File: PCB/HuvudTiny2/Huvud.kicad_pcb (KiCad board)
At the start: 4 copper layers, 42 x 42 mm, 99 parts, among them J1 Vin, J12 USB_Micro-B, J2 DBG, J3 THERM, J4 FAN0, J5 FAN1, J6 Heater, J7 Endstop, J9 STEPPER, Q1 AO3400A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

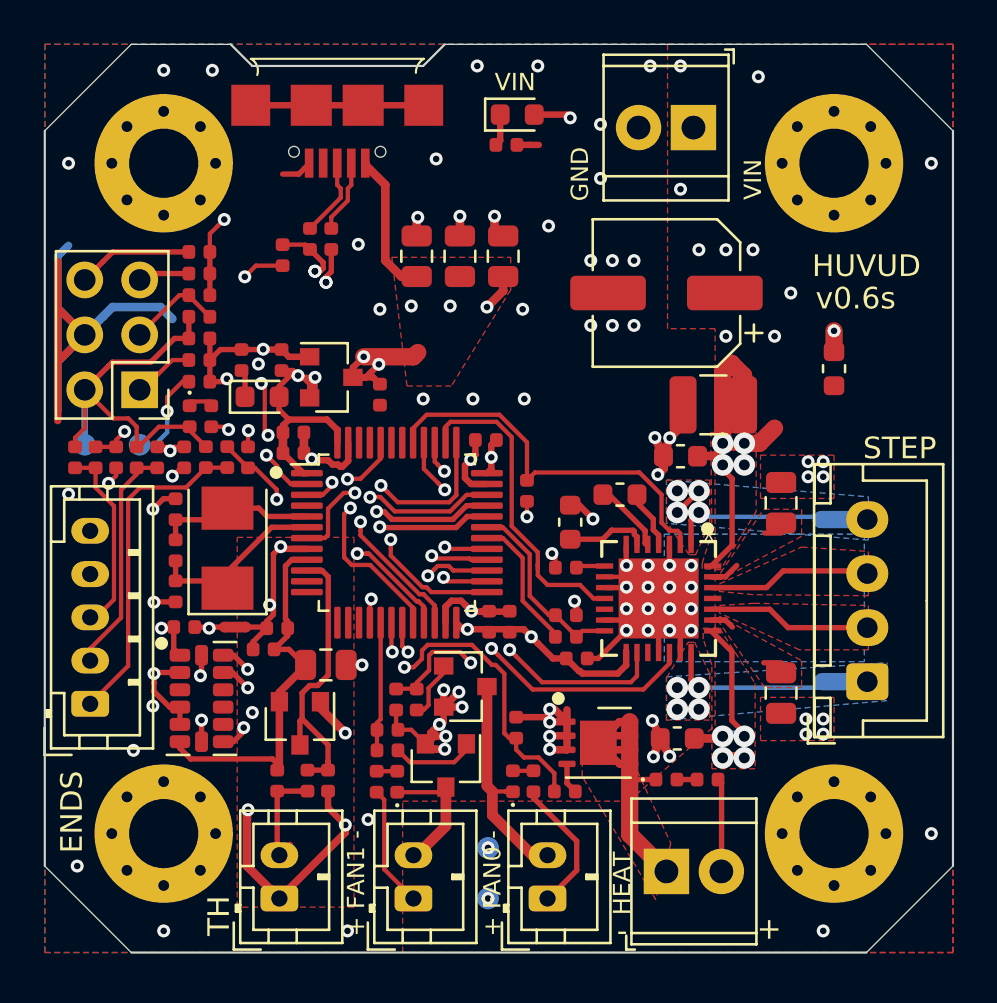
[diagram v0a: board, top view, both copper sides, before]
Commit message: Add protection diode on endstop 1. Add back heatsink for power mosfet.
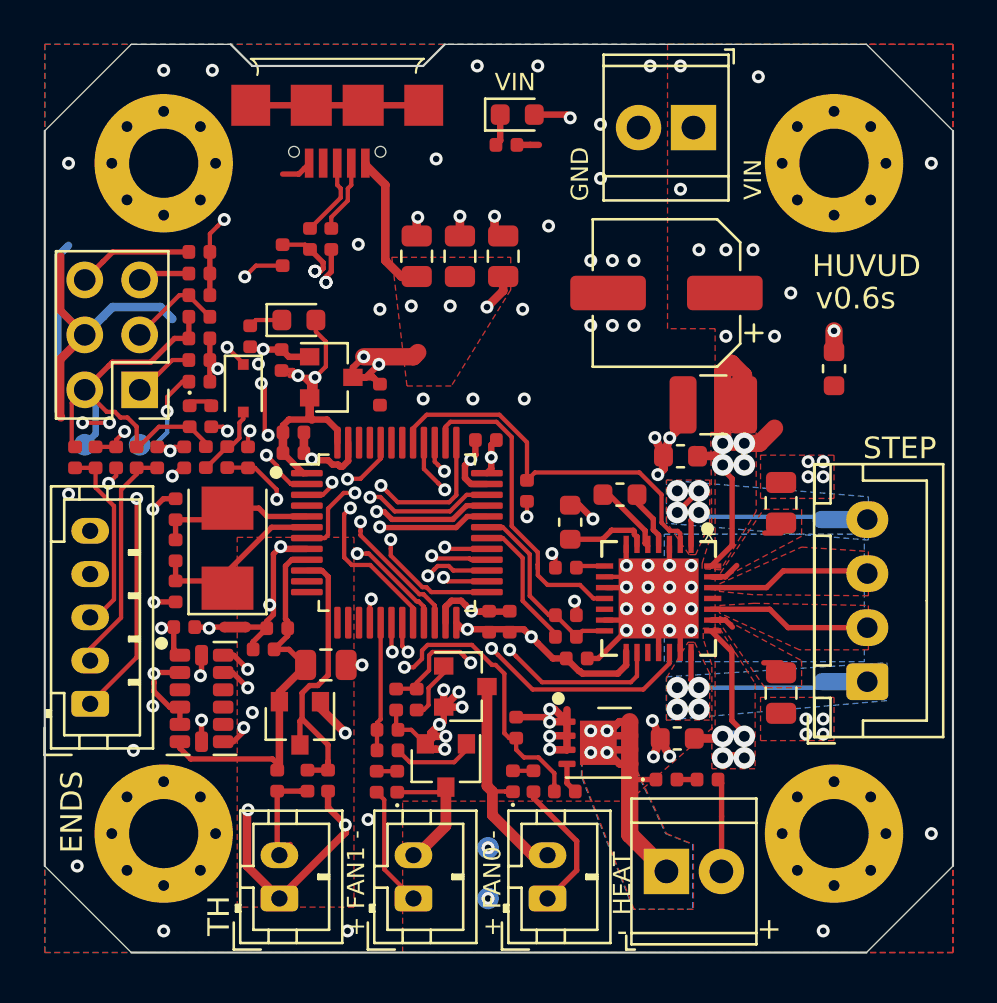
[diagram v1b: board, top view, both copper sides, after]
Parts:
- added D4: PMEG6010CEJ, Diode_SMD:D_SOD-323F, F.Cu at (191.2, 115.9)
- moved D8 3.94 mm to (193.8, 112.8)
- moved R20 1.17 mm to (191.5, 113.5), turned to -90 degrees
- turned R32 to -90 degrees
- turned R33 to -90 degrees
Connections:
- J7 pad 1: Net-(J7-Pad1) -> Net-(D4-Pad1)
- R32 pad 1: Net-(J7-Pad1) -> +3V3
- R32 pad 2: +3V3 -> Net-(D4-Pad2)
- R33 pad 1: Net-(J7-Pad1) -> Net-(D4-Pad2)
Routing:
- net Net-(D4-Pad1): track 0.00 -> 32.0 mm, vias 0 -> 4
- net Net-(J7-Pad1): track 15.4 -> 0.00 mm
- net GND: track 122.3 -> 116.9 mm
- net Net-(D4-Pad2): track 0.00 -> 3.40 mm
- net +3V3: track 85.3 -> 87.7 mm
- net SWCLK: track 32.3 -> 33.0 mm
- net Net-(D3-Pad1): vias 0 -> 4
- added copper zone on B.Cu, net Net-(D3-Pad1)

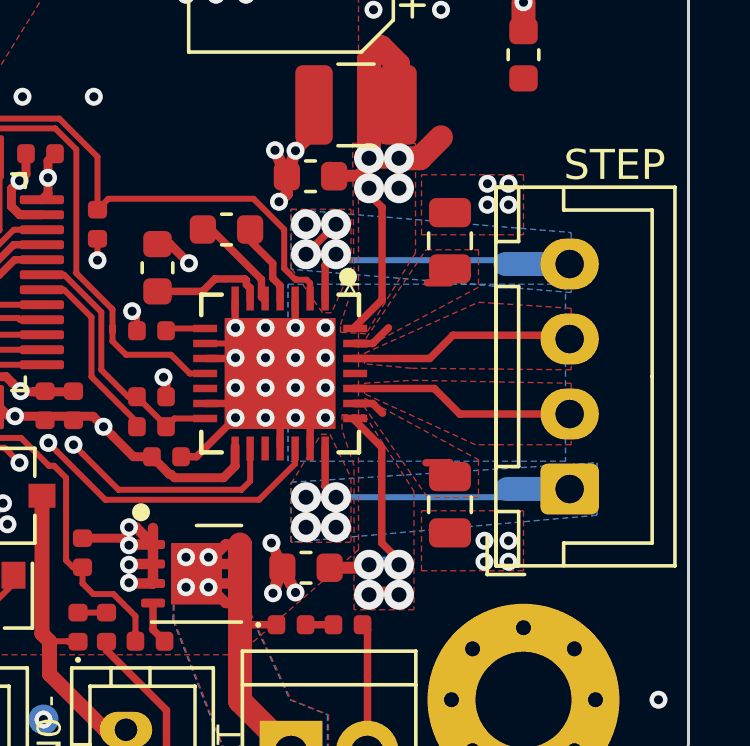
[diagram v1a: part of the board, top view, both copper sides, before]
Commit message: Update sense resistors to 0.1 1206 size.
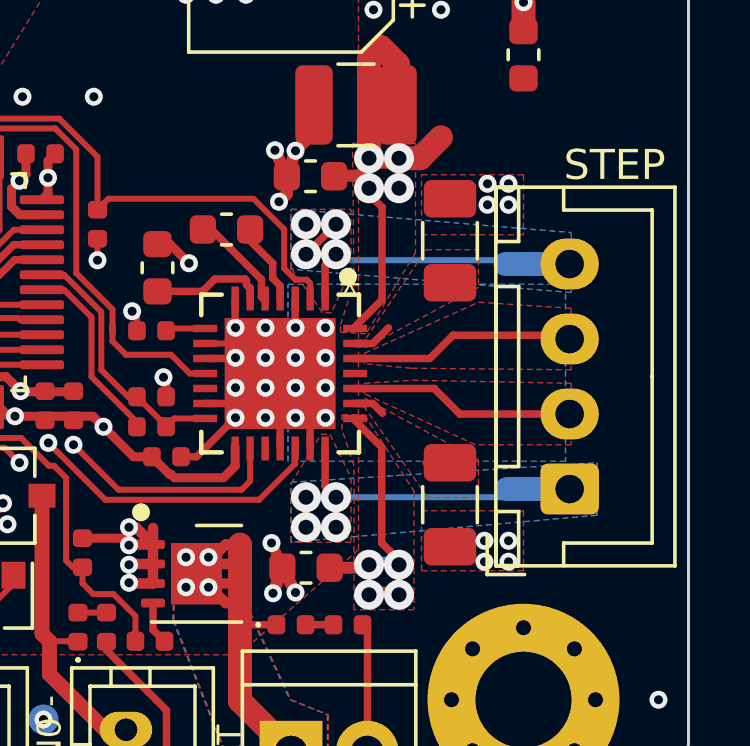
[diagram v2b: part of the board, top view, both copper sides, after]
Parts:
- R4, R7: value 0.110 1% -> 0.1 1%; footprint Resistor_SMD:R_0805_2012Metric -> Resistor_SMD:R_1206_3216Metric
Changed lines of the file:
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@@
     )
   )
-  (footprint "Resistor_SMD:R_0805_2012Metric" (layer "F.Cu")
+  (footprint "Resistor_SMD:R_1206_3216Metric" (layer "F.Cu")
     (at 216.05 121.2 -90)
-    (descr "Resistor SMD 0805 (2012 Metric), square (rectangular) end terminal, IPC_7351 nominal, (Body size source: https://docs.google.com/spreadsheets/d/1BsfQQcO9C6DZCsRaXUlFlo91Tg2WpOkGARC1WS5S8t0/edit?usp=sharing), generated with kicad-footprint-generator")
+    (descr "Resistor SMD 1206 (3216 Metric), square (rectangular) end terminal, IPC_7351 nominal, (Body size source: http://www.tortai-tech.com/upload/download/2011102023233369053.pdf), generated with kicad-footprint-generator")
     (tags "resistor")
-    (property "LCSC" "C53899")
-    (property "Sheetfile" "Huvud.kicad_sch")
-    (property "Sheetname" "")
-    (attr smd)
-    (fp_text reference "R7" (at 0 -1.65 -90) (layer "F.SilkS") hide
-      (effects (font (size 1 1) (thickness 0.15)))
-    )
-    (fp_text value "0.110 1%" (at 0 1.65 -90) (layer "F.Fab")
+    (property "LCSC" "C25334")
+    (property "Sheetfile" "Huvud.kicad_sch")
+    (property "Sheetname" "")
+    (attr smd)
+    (fp_text reference "R7" (at 0 -1.82 -90) (layer "F.SilkS") hide
+      (effects (font (size 1 1) (thickness 0.15)))
+    )
+    (fp_text value "0.1 1%" (at 0 1.82 -90) (layer "F.Fab")
       (effects (font (size 1 1) (thickness 0.15)))
     )
     (fp_text user "${REFERENCE}" (at 0 0 -90) (layer "F.Fab")
-      (effects (font (size 0.5 0.5) (thickness 0.08)))
-    )
-    (fp_line (start -0.258578 -0.71) (end 0.258578 -0.71) (layer "F.SilkS") (width 0.12))
-    (fp_line (start -0.258578 0.71) (end 0.258578 0.71) (layer "F.SilkS") (width 0.12))
-    (fp_line (start 1.68 0.95) (end -1.68 0.95) (layer "F.CrtYd") (width 0.05))
-    (fp_line (start 1.68 -0.95) (end 1.68 0.95) (layer "F.CrtYd") (width 0.05))
-    (fp_line (start -1.68 -0.95) (end 1.68 -0.95) (layer "F.CrtYd") (width 0.05))
-    (fp_line (start -1.68 0.95) (end -1.68 -0.95) (layer "F.CrtYd") (width 0.05))
-    (fp_line (start 1 0.6) (end -1 0.6) (layer "F.Fab") (width 0.1))
-    (fp_line (start -1 -0.6) (end 1 -0.6) (layer "F.Fab") (width 0.1))
-    (fp_line (start -1 0.6) (end -1 -0.6) (layer "F.Fab") (width 0.1))
-    (fp_line (start 1 -0.6) (end 1 0.6) (layer "F.Fab") (width 0.1))
-    (pad "1" smd roundrect locked (at -0.9375 0 270) (size 0.975 1.4) (layers "F.Cu" "F.Paste" "F.Mask") (roundrect_rratio 0.25)
+      (effects (font (size 0.8 0.8) (thickness 0.12)))
+    )
+    (fp_line (start -0.602064 -0.91) (end 0.602064 -0.91) (layer "F.SilkS") (width 0.12))
+    (fp_line (start -0.602064 0.91) (end 0.602064 0.91) (layer "F.SilkS") (width 0.12))
+    (fp_line (start 2.28 -1.12) (end 2.28 1.12) (layer "F.CrtYd") (width 0.05))
+    (fp_line (start 2.28 1.12) (end -2.28 1.12) (layer "F.CrtYd") (width 0.05))
+    (fp_line (start -2.28 -1.12) (end 2.28 -1.12) (layer "F.CrtYd") (width 0.05))
+    (fp_line (start -2.28 1.12) (end -2.28 -1.12) (layer "F.CrtYd") (width 0.05))
+    (fp_line (start -1.6 0.8) (end -1.6 -0.8) (layer "F.Fab") (width 0.1))
+    (fp_line (start 1.6 -0.8) (end 1.6 0.8) (layer "F.Fab") (width 0.1))
+    (fp_line (start -1.6 -0.8) (end 1.6 -0.8) (layer "F.Fab") (width 0.1))
+    (fp_line (start 1.6 0.8) (end -1.6 0.8) (layer "F.Fab") (width 0.1))
+    (pad "1" smd roundrect locked (at -1.4 0 270) (size 1.25 1.75) (layers "F.Cu" "F.Paste" "F.Mask") (roundrect_rratio 0.2)
       (net 2 "GND") (pintype "passive"))
-    (pad "2" smd roundrect locked (at 0.9375 0 270) (size 0.975 1.4) (layers "F.Cu" "F.Paste" "F.Mask") (roundrect_rratio 0.25)
+    (pad "2" smd roundrect locked (at 1.4 0 270) (size 1.25 1.75) (layers "F.Cu" "F.Paste" "F.Mask") (roundrect_rratio 0.2)
       (net 32 "BRB") (pintype "passive"))
-    (model "${KISYS3DMOD}/Resistor_SMD.3dshapes/R_0805_2012Metric.wrl"
-      (offset (xyz 0 0 0))
-      (scale (xyz 1 1 1))
-      (rotate (xyz 0 0 0))
-    )
-  )
-  (footprint "Resistor_SMD:R_0805_2012Metric" (layer "F.Cu")
+    (model "${KISYS3DMOD}/Resistor_SMD.3dshapes/R_1206_3216Metric.wrl"
+      (offset (xyz 0 0 0))
+      (scale (xyz 1 1 1))
+      (rotate (xyz 0 0 0))
+    )
+  )
+  (footprint "Resistor_SMD:R_1206_3216Metric" (layer "F.Cu")
     (at 216.05 130 90)
-    (descr "Resistor SMD 0805 (2012 Metric), square (rectangular) end terminal, IPC_7351 nominal, (Body size source: https://docs.google.com/spreadsheets/d/1BsfQQcO9C6DZCsRaXUlFlo91Tg2WpOkGARC1WS5S8t0/edit?usp=sharing), generated with kicad-footprint-generator")
+    (descr "Resistor SMD 1206 (3216 Metric), square (rectangular) end terminal, IPC_7351 nominal, (Body size source: http://www.tortai-tech.com/upload/download/2011102023233369053.pdf), generated with kicad-footprint-generator")
     (tags "resistor")
-    (property "LCSC" "C53899")
-    (property "Sheetfile" "Huvud.kicad_sch")
-    (property "Sheetname" "")
-    (attr smd)
-    (fp_text reference "R4" (at 0 -1.65 90) (layer "F.SilkS") hide
-      (effects (font (size 1 1) (thickness 0.15)))
-    )
-    (fp_text value "0.110 1%" (at 0 1.65 90) (layer "F.Fab")
+    (property "LCSC" "C25334")
+    (property "Sheetfile" "Huvud.kicad_sch")
+    (property "Sheetname" "")
+    (attr smd)
+    (fp_text reference "R4" (at 0 -1.82 90) (layer "F.SilkS") hide
+      (effects (font (size 1 1) (thickness 0.15)))
+    )
+    (fp_text value "0.1 1%" (at 0 1.82 90) (layer "F.Fab")
       (effects (font (size 1 1) (thickness 0.15)))
     )
     (fp_text user "${REFERENCE}" (at 0 0 90) (layer "F.Fab")
-      (effects (font (size 0.5 0.5) (thickness 0.08)))
-    )
-    (fp_line (start -0.258578 -0.71) (end 0.258578 -0.71) (layer "F.SilkS") (width 0.12))
-    (fp_line (start -0.258578 0.71) (end 0.258578 0.71) (layer "F.SilkS") (width 0.12))
-    (fp_line (start -1.68 -0.95) (end 1.68 -0.95) (layer "F.CrtYd") (width 0.05))
-    (fp_line (start -1.68 0.95) (end -1.68 -0.95) (layer "F.CrtYd") (width 0.05))
-    (fp_line (start 1.68 0.95) (end -1.68 0.95) (layer "F.CrtYd") (width 0.05))
-    (fp_line (start 1.68 -0.95) (end 1.68 0.95) (layer "F.CrtYd") (width 0.05))
-    (fp_line (start -1 -0.6) (end 1 -0.6) (layer "F.Fab") (width 0.1))
-    (fp_line (start 1 0.6) (end -1 0.6) (layer "F.Fab") (width 0.1))
-    (fp_line (start -1 0.6) (end -1 -0.6) (layer "F.Fab") (width 0.1))
-    (fp_line (start 1 -0.6) (end 1 0.6) (layer "F.Fab") (width 0.1))
-    (pad "1" smd roundrect locked (at -0.9375 0 90) (size 0.975 1.4) (layers "F.Cu" "F.Paste" "F.Mask") (roundrect_rratio 0.25)
+      (effects (font (size 0.8 0.8) (thickness 0.12)))
+    )
+    (fp_line (start -0.602064 -0.91) (end 0.602064 -0.91) (layer "F.SilkS") (width 0.12))
+    (fp_line (start -0.602064 0.91) (end 0.602064 0.91) (layer "F.SilkS") (width 0.12))
+    (fp_line (start -2.28 -1.12) (end 2.28 -1.12) (layer "F.CrtYd") (width 0.05))
+    (fp_line (start 2.28 1.12) (end -2.28 1.12) (layer "F.CrtYd") (width 0.05))
+    (fp_line (start 2.28 -1.12) (end 2.28 1.12) (layer "F.CrtYd") (width 0.05))
+    (fp_line (start -2.28 1.12) (end -2.28 -1.12) (layer "F.CrtYd") (width 0.05))
+    (fp_line (start -1.6 0.8) (end -1.6 -0.8) (layer "F.Fab") (width 0.1))
+    (fp_line (start 1.6 0.8) (end -1.6 0.8) (layer "F.Fab") (width 0.1))
+    (fp_line (start -1.6 -0.8) (end 1.6 -0.8) (layer "F.Fab") (width 0.1))
+    (fp_line (start 1.6 -0.8) (end 1.6 0.8) (layer "F.Fab") (width 0.1))
+    (pad "1" smd roundrect locked (at -1.4 0 90) (size 1.25 1.75) (layers "F.Cu" "F.Paste" "F.Mask") (roundrect_rratio 0.2)
       (net 2 "GND") (pintype "passive"))
-    (pad "2" smd roundrect locked (at 0.9375 0 90) (size 0.975 1.4) (layers "F.Cu" "F.Paste" "F.Mask") (roundrect_rratio 0.25)
+    (pad "2" smd roundrect locked (at 1.4 0 90) (size 1.25 1.75) (layers "F.Cu" "F.Paste" "F.Mask") (roundrect_rratio 0.2)
       (net 31 "BRA") (pintype "passive"))
-    (model "${KISYS3DMOD}/Resistor_SMD.3dshapes/R_0805_2012Metric.wrl"
+    (model "${KISYS3DMOD}/Resistor_SMD.3dshapes/R_1206_3216Metric.wrl"
       (offset (xyz 0 0 0))
       (scale (xyz 1 1 1))
@@
     (fp_line (start -0.5 0.25) (end -0.5 -0.25) (layer "F.Fab") (width 0.1))
     (pad "1" smd roundrect locked (at -0.485 0 270) (size 0.59 0.64) (layers "F.Cu" "F.Paste" "F.Mask") (roundrect_rratio 0.25)
-      (net 8 "+3V3"))
+      (net 8 "+3V3") (pintype "passive"))
     (pad "2" smd roundrect locked (at 0.485 0 270) (size 0.59 0.64) (layers "F.Cu" "F.Paste" "F.Mask") (roundrect_rratio 0.25)
-      (net 65 "Net-(D4-Pad2)"))
+      (net 65 "Net-(D4-Pad2)") (pintype "passive"))
     (model "${KISYS3DMOD}/Resistor_SMD.3dshapes/R_0402_1005Metric.wrl"
       (offset (xyz 0 0 0))

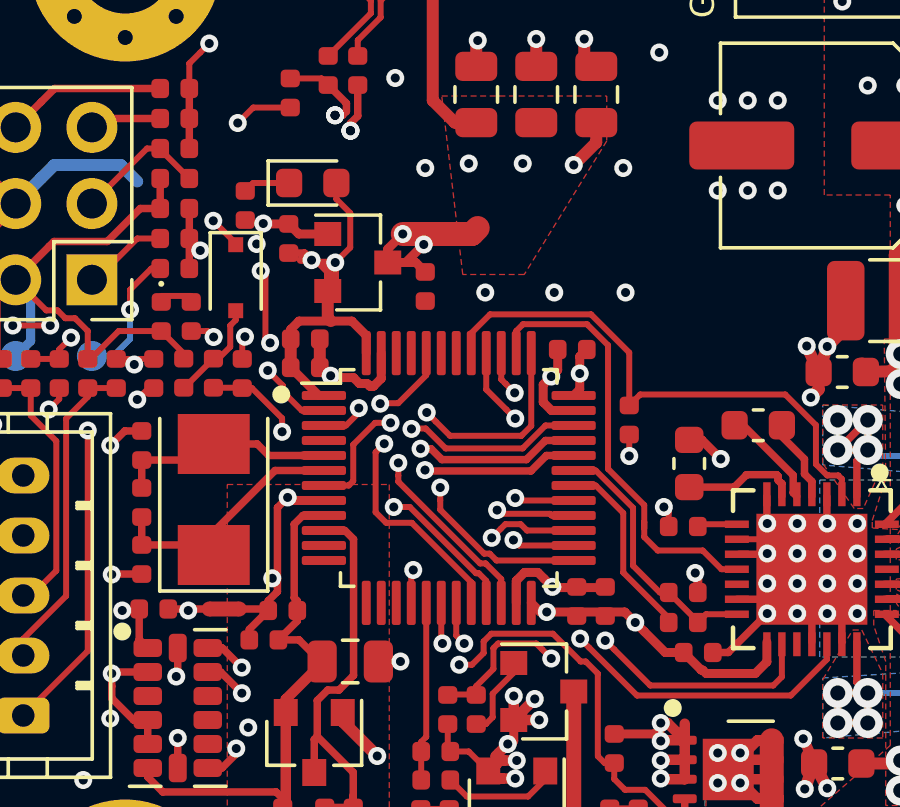
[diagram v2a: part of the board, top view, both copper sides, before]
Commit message: Route VCC_IO to GPIO pin so we can reset the stepper driver.
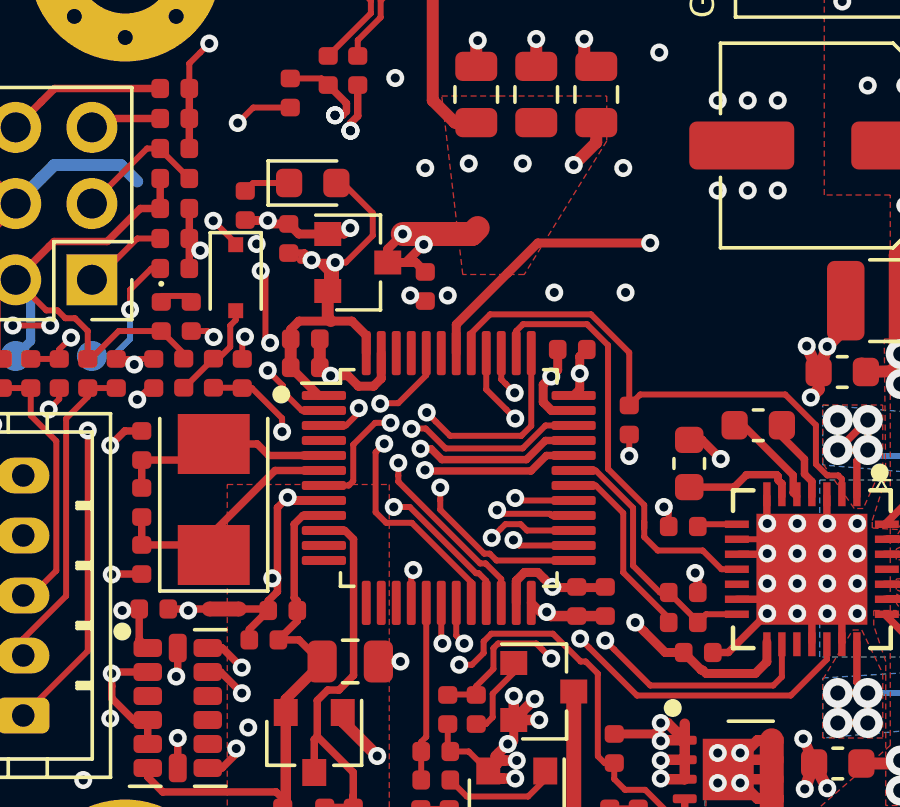
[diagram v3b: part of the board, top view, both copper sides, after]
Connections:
- C9 pad 2: +3V3 -> VCC_IO
- U2 pad 15: +3V3 -> VCC_IO
- U5 pad 42: (no net) -> VCC_IO
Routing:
- net VCC_IO: track 0.00 -> 27.3 mm, vias 0 -> 2
- net +3V3: track 87.7 -> 81.7 mm, vias 8 -> 7
- net GND: track 116.9 -> 118.4 mm, vias 90 -> 92

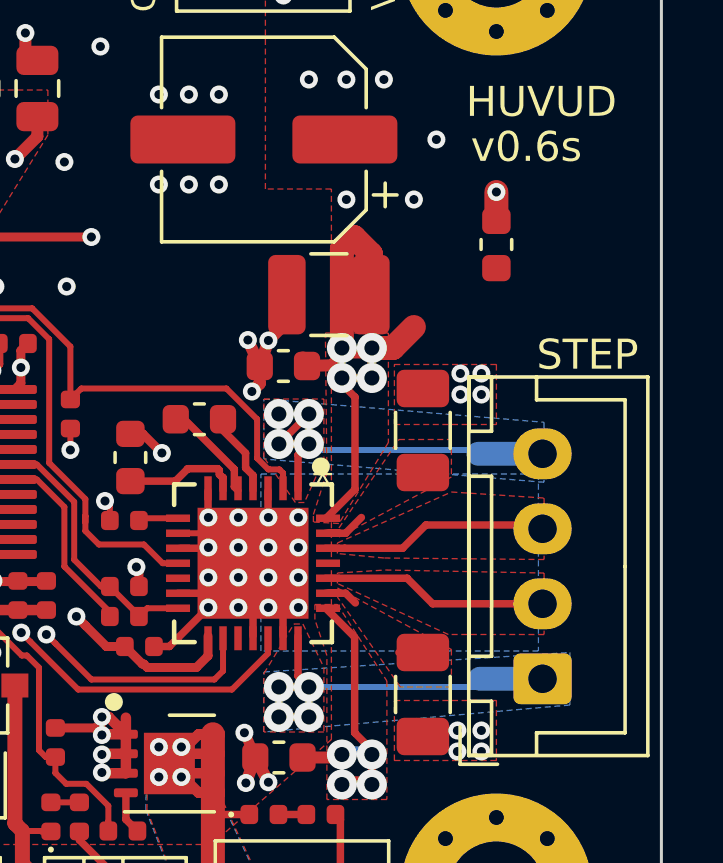
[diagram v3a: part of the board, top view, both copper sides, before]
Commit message: Added caps across stepper pins.
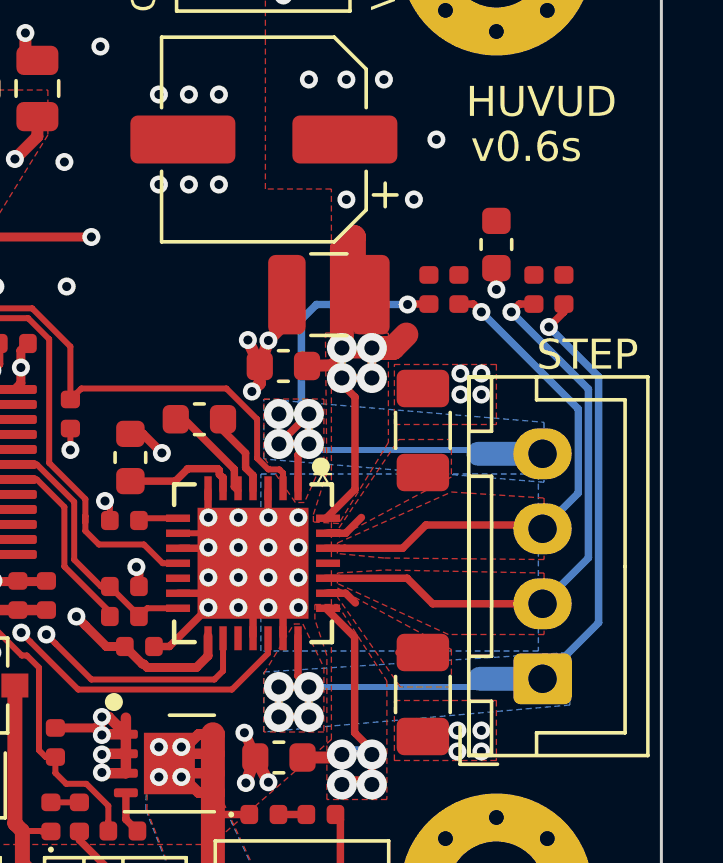
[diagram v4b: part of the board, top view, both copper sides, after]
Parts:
- added C20: 1nF 50V, Capacitor_SMD:C_0402_1005Metric, F.Cu at (216.2, 116.5)
- added C21: 1nF 50V, Capacitor_SMD:C_0402_1005Metric, F.Cu at (217.2, 116.5)
- added C26: 1nF 50V, Capacitor_SMD:C_0402_1005Metric, F.Cu at (220.8, 116.5)
- added C28: 1nF 50V, Capacitor_SMD:C_0402_1005Metric, F.Cu at (219.8, 116.5)
- turned C16 to -90 degrees
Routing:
- net /ST_A2: track 15.8 -> 29.9 mm, vias 4 -> 5
- net /ST_A1: track 7.53 -> 19.8 mm, vias 0 -> 1
- net /ST_B1: track 7.55 -> 17.5 mm, vias 0 -> 1
- net /ST_B2: track 15.1 -> 22.8 mm, vias 4 -> 5
- net ST_VS: track 48.1 -> 46.3 mm
